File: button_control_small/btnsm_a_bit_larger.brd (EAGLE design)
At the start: 19 x 14.9 mm, 18 parts, among them IC1 TINY13V-10SSU, Q1 IRF8788

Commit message: Added version for heater canister
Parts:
- added LED1, LED3: (no value), eagle-ltspice:LED_SML0603
- added LED2, LED4: (no value), led:LED5MM
- added R3: 300, rcl:R0402
- moved OUT- 34.9 mm to (28.0, 34.5), turned to 180 degrees
- moved PAD2 34.9 mm to (30.7, 24.2), flipped to the bottom
- moved Q1 32.6 mm to (29.0, 30.3), flipped to the bottom, turned to 90 degrees
- moved IN- 24.6 mm to (28.0, 27.0), turned to 90 degrees
- moved C1 23.3 mm to (11.1, 33.3), flipped to the bottom
- moved R1 22.3 mm to (12.5, 31.2), flipped to the bottom, turned to 0 degrees
- moved R2 22.1 mm to (8.86, 31.2), flipped to the bottom, turned to 0 degrees
- moved IN+ 21.7 mm to (12.0, 34.5), turned to 180 degrees
- moved IC1 21.2 mm to (11.3, 26.8), flipped to the bottom
- moved C2 20.8 mm to (21.7, 27.0), flipped to the bottom, turned to 90 degrees
- moved PAD6 20.1 mm to (30.7, 22.0)
- moved PAD4 19.8 mm to (5.80, 31.6), flipped to the bottom
- moved PAD5 19.7 mm to (2.40, 23.9), flipped to the bottom
- moved PAD3 19.4 mm to (2.40, 21.9), flipped to the bottom
- moved U$3 18.3 mm to (19.6, 27.1), flipped to the bottom, turned to 270 degrees
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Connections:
- new net N$6: LED1.A, LED2.A, LED3.A, LED4.A, R3.2
- net N$3: now also R3.1
- net N$4: now also LED1.C, LED2.K, LED3.C, LED4.K
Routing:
- net N$4: track 13.5 -> 71.3 mm, vias 0 -> 5
- net N$6: track 0.00 -> 53.0 mm, vias 0 -> 2
- net N$2: track 2.28 -> 38.0 mm, vias 0 -> 2
- net VDD: track 14.7 -> 46.7 mm, vias 0 -> 1
- net N$3: track 9.79 -> 31.2 mm, vias 0 -> 2
- net MISO: track 2.19 -> 21.1 mm, vias 0 -> 1
- net GND: track 42.6 -> 57.9 mm, vias 0 -> 3
- net N$1: track 12.7 -> 1.72 mm
- net MOSI: track 1.89 -> 12.8 mm
- net SCK: track 2.64 -> 9.45 mm
- added copper zone on layer 16, net GND
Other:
- board size 19 x 14.9 mm -> 39.2 x 25.5 mm
- board text added: "+"
- board text added: "-"
- board text added: "B+"
- board text added: "B-"
- board text added: "BTN/GND"
- board text added: "BTN/MISO"
- board text added: "MOSI"
- board text added: "RST"
- board text added: "SCK"
- board text added: "VDD"

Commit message: Add files via upload
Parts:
- removed IC1: TINY13V-10SSU, atmel:8S1
- removed LED1, LED3: (no value), eagle-ltspice:LED_SML0603
- removed LED2, LED4: (no value), led:LED5MM
- removed PAD1, PAD2, PAD3, PAD4, PAD5, PAD6: (no value), wirepad:1,6/0,9
- added BTN1: BTN1, wirepad:1,6/0,9
- added BTN2: BNT2, wirepad:1,6/0,9
- added C4, C5: 100n, resistor:C0603
- added D1: (no value), SparkFun-LED:LED-TRICOLOR-5050
- added IC2: MEGA8-AI, atmel:TQFP32-08
- added J1: AVR_SPI_PROG_3X2NS, SparkFun-Connectors:2X3-NS
- added R10: 100k, rcl:R0402
- added R4, R5: 470, rcl:R0402
- added R6: 520, rcl:R0402
- added R7: 282k, rcl:R0402
- added R8: 470k, rcl:R0402
- added R9: 2.2k, rcl:R0402
- added RX: RX, wirepad:1,6/0,9
- added T1, T2: BC848, transistor-neu-to92:SOT23
- added TX: TX, wirepad:1,6/0,9
- added WTR: WATER, wirepad:1,6/0,9
- C2: value 0.33uF -> 100n
- C3: value 2.2uF -> 1uF; device resistor:C0603 -> resistor:C0805
- R3: value 300 -> 100k
- U$3: value TPS71550 -> TPS71533
- moved IN+ 26.2 mm to (36.0, 24.0), turned to 0 degrees
- moved OUT- 26.2 mm to (4.00, 24.0)
- moved R3 21.5 mm to (24.9, 28.7), flipped to the top, turned to 90 degrees
- moved Q1 20.3 mm to (9.88, 23.7), flipped to the top, turned to 180 degrees
- moved IN- 18.8 mm to (11.0, 19.0)
- moved OUT+ 18.7 mm to (28.9, 19.1)
- moved C3 13.9 mm to (31.3, 25.7), flipped to the top
- moved C1 9.64 mm to (10.1, 23.7), turned to 270 degrees
- moved U$3 9.62 mm to (29.1, 25.6), flipped to the top
- moved R2 7.99 mm to (11.7, 23.7), turned to 270 degrees
- moved R1 7.43 mm to (15.5, 24.4), flipped to the top, turned to 270 degrees
- moved C2 5.41 mm to (26.9, 25.5), flipped to the top
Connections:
- removed net N$1: IC1.3, R1.2
- removed net N$3: C2.1, IN+.1, OUT+.1, R3.1, U$3.4
- new net ADC0: IC2.23, R3.1, R7.2
- new net AREF: C5.2, IC2.20
- new net BTN1: BTN1.1, IC2.32
- new net N$13: T1.2, T2.1
- new net N$16: R10.2, R8.1, WTR.1
- new net N$17: R10.1, T1.1
- new net N$18: R9.1, T1.3
- new net N$7: D1.6, R4.2
- new net N$8: D1.4, R5.2
- new net PWM0: D1.3, IC2.10
- new net PWM1: D1.1, IC2.14
- new net PWM2: D1.2, IC2.13
- new net RX: IC2.30, R1.2, RX.1
- new net TX: IC2.31, TX.1
- new net VIN: C2.1, IN+.1, OUT+.1, R4.1, R5.1, R6.1, R7.1, R9.2, U$3.4
- new net WTR: IC2.1, T2.3
- net GND: now also BTN2.1, C4.2, C5.1, IC2.21, IC2.3, IC2.5, J1.6, R8.2, T2.2; no longer IC1.4, PAD6.1
- net MISO: now also IC2.16, J1.1; no longer IC1.6, PAD2.1
- net MOSI: now also IC2.15, J1.4; no longer IC1.5, PAD1.1
- net N$4: now also R3.2; no longer LED1.C, LED2.K, LED3.C, LED4.K
- net N$6: now also D1.5, R6.2; no longer LED1.A, LED2.A, LED3.A, LED4.A, R3.2
- net RST: now also IC2.29, J1.5; no longer IC1.1, PAD4.1
- net SCK: now also IC2.17, J1.3; no longer IC1.7, PAD3.1
- net VDD: now also C4.1, IC2.18, IC2.4, IC2.6, J1.2; no longer IC1.8, PAD5.1
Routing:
- net GND: track 57.9 -> 122.3 mm, vias 3 -> 2
- net MOSI: track 12.8 -> 66.4 mm
- net N$6: track 53.0 -> 4.80 mm, vias 2 -> 0
- net VIN: track 0.00 -> 39.1 mm, vias 0 -> 1
- net N$4: track 71.3 -> 35.5 mm, vias 5 -> 0
- net N$2: track 38.0 -> 3.09 mm, vias 2 -> 0
- net PWM1: track 0.00 -> 32.5 mm
- net RX: track 0.00 -> 32.3 mm, vias 0 -> 1
- net RST: track 8.76 -> 40.9 mm, vias 0 -> 2
- net N$3: track 31.2 -> 0.00 mm, vias 2 -> 0
- net PWM2: track 0.00 -> 30.7 mm
- net PWM0: track 0.00 -> 30.1 mm
- net MISO: track 21.1 -> 49.4 mm, vias 1 -> 0
- net ADC0: track 0.00 -> 28.1 mm, vias 0 -> 3
- net WTR: track 0.00 -> 25.9 mm, vias 0 -> 2
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- removed copper zone on layer 16, net GND
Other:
- board size 39.2 x 25.5 mm -> 41.4 x 41.4 mm
- board text removed: "BTN/GND"
- board text removed: "BTN/MISO"
- board text removed: "MOSI"
- board text removed: "RST"
- board text removed: "SCK"
- board text removed: "VDD"

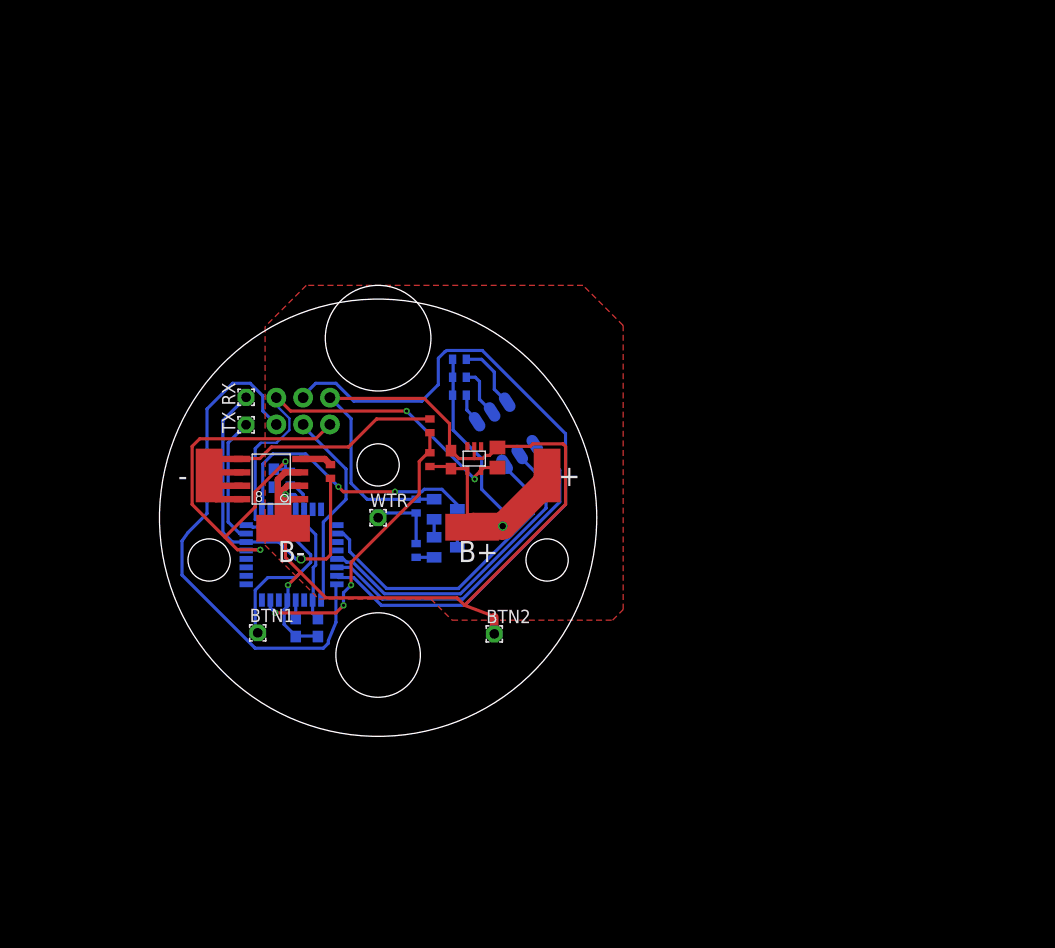
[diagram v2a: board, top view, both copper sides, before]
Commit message: Add files via upload
Developing a new version with better power consumption and capabilities
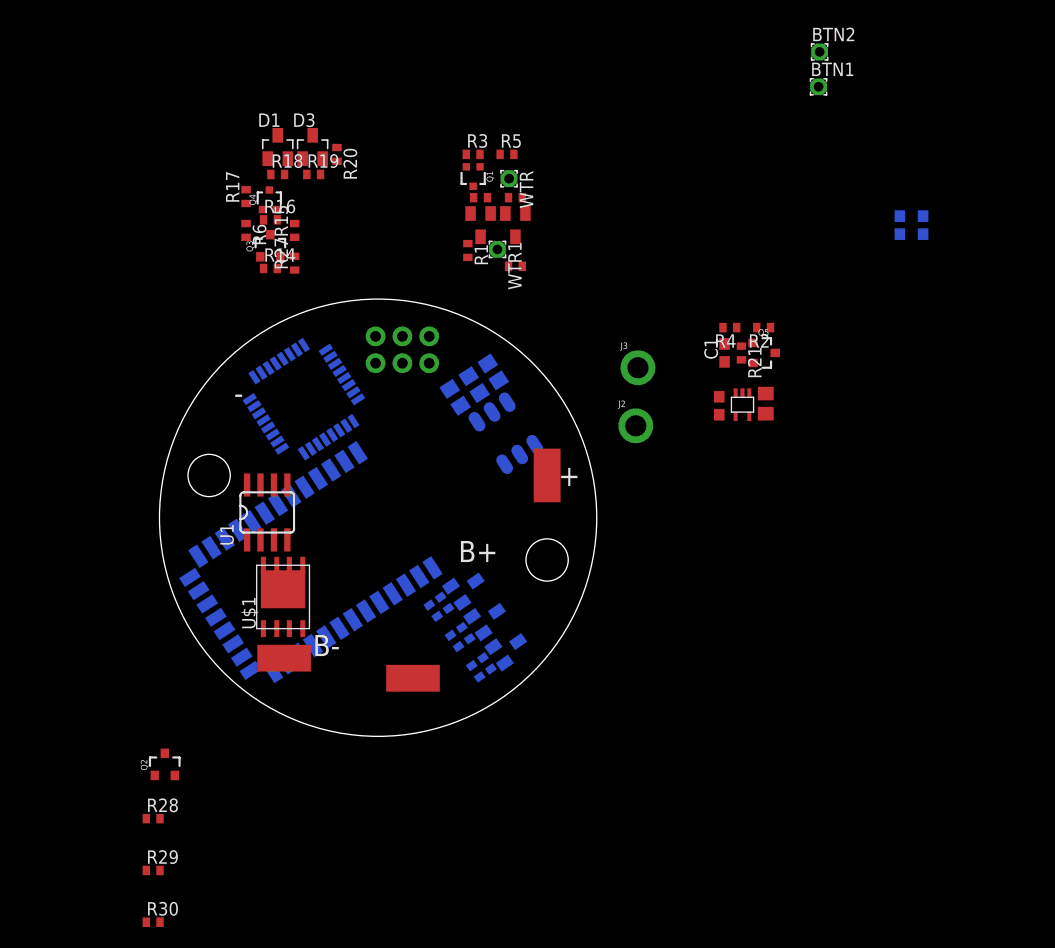
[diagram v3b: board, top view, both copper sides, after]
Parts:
- removed OUT-: OUT-, wirepad:SMD2,54-5,08
- removed RX: RX, wirepad:1,6/0,9
- removed TX: TX, wirepad:1,6/0,9
- added D2: (no value), SparkFun-LED:LED-TRICOLOR-5050
- added D3: BAT54, diode:SOT23
- added J2: OUT-, SparkFun-Connectors:1X01_2MM
- added J3: OUT+, SparkFun-Connectors:1X01_2MM
- added Q2, Q3, Q5: IRLML9301, SparkFun-DiscreteSemi:SOT23-3
- added Q4: 2N2007 (SOT323), SparkFun-DiscreteSemi:SOT323
- added R11, R12: 470, rcl:R0805
- added R13: 520, rcl:R0805
- added R14, R15, R16, R17, R20, R21, R22, R23, R28, R29, R30: 100k, rcl:R0402
- added R18, R19, R24, R25, R26, R27: 200, rcl:R0402
- added T3, T4, T5: BC848, transistor-neu-to92:SOT23
- added U$1: IRFH6200, IRFH6200:PQFN
- added U1: ACS711ELCTR-25AB-T, allegro:SOIC8
- added U2: HC_05, Bluetooth HC-05:BLUETOOTH_SMD
- added WTR1: WTR-PWR, wirepad:1,6/0,9
- D1: value (none) -> BAT54; device SparkFun-LED:LED-TRICOLOR-5050 -> diode:SOT23
- Q1: value IRF8788 -> 2N2007 (SOT323); device transistor-fet:SO-8 -> SparkFun-DiscreteSemi:SOT323
- R1: value 100R -> 100k
- R2: value 10K -> 282k
- R4: value 470 -> 100k
- R5: value 470 -> 200
- R6: value 520 -> 200
- R7: value 282k -> 100k
- WTR: value WATER -> WTR-IN
- moved BTN1 74.1 mm to (61.7, 60.8)
- moved C4 68.8 mm to (71.6, 47.7)
- moved C5 68.7 mm to (69.4, 47.7)
- moved BTN2 63.1 mm to (61.8, 64.1)
- moved R2 47.0 mm to (56.5, 38.0), flipped to the top, turned to 180 degrees
- moved C1 44.3 mm to (52.8, 35.6), flipped to the top, turned to 90 degrees
- moved R10 34.7 mm to (33.0, 50.3), flipped to the top, turned to 180 degrees
- moved D1 34.7 mm to (10.5, 55.1), flipped to the top, turned to 0 degrees
- moved Q1 34.4 mm to (29.0, 52.3)
- moved WTR 34.4 mm to (32.4, 52.1), turned to 270 degrees
- moved T1 31.2 mm to (33.0, 47.7), flipped to the top, turned to 180 degrees
- moved R8 29.8 mm to (29.7, 50.3), flipped to the top, turned to 180 degrees
- moved T2 27.1 mm to (29.7, 47.7), flipped to the top, turned to 180 degrees
- moved R3 26.0 mm to (29.0, 54.4), turned to 0 degrees
- moved C3 25.9 mm to (56.7, 30.8)
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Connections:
- removed net ADC0: IC2.23, R3.1, R7.2
- removed net PWM1: D1.1, IC2.14
- removed net PWM2: D1.2, IC2.13
- removed net RX: IC2.30, R1.2, RX.1
- removed net TX: IC2.31, TX.1
- removed net VIN: C2.1, IN+.1, OUT+.1, R4.1, R5.1, R6.1, R7.1, R9.2, U$3.4
- new net +12V: C2.1, IN+.1, OUT+.1, Q5.2, R11.1, R12.1, R13.1, R21.2, R27.1, R9.2, U$3.4, WTR1.1
- new net N$1: D2.2, R13.2
- new net N$10: Q4.1, R16.1, R18.2, R6.1
- new net N$11: C1.2, Q5.1, R21.1
- new net N$12: Q4.3, R17.2
- new net N$14: C1.1, IC2.24
- new net N$15: D1.1, R18.1
- new net N$19: D3.1, R19.1
- new net N$20: D1.3, D3.3, R20.1, U$1.4
- new net N$21: IC2.25, R19.2
- new net N$22: IC2.23, R2.2, R4.1
- new net N$23: Q5.3, R2.1
- new net N$24: D2.4, T5.3
- new net N$25: D2.6, T4.3
- new net N$26: D2.5, T3.3
- new net N$27: R23.1, R26.2, T5.1
- new net N$28: R22.1, R25.2, T4.1
- new net N$29: R24.2, R7.1, T3.1
- new net N$3: D2.3, R11.2
- new net N$30: IC2.14, R24.1
- new net N$31: IC2.13, R25.1
- new net N$32: Q3.2, R14.2, R27.2
- new net N$33: Q2.1, R28.1
- new net N$34: J2.1, U1.1, U1.2
- new net N$35: R29.2, R30.1
- new net N$36: Q2.3, R29.1, U1.8
- new net N$37: U1.7
- new net N$5: D2.1, R12.2
- new net N$9: Q3.3, R15.1, R6.2
- net GND: now also Q4.2, R15.2, R16.2, R20.2, R22.2, R23.2, R3.1, R30.2, R4.2, R7.2, T3.2, T4.2, T5.2, U$1.1, U$1.2, U$1.3, U1.5; no longer C1.2, Q1.1, Q1.3, R8.2, T2.2
- net N$2: now also T2.3; no longer Q1.4
- net N$4: now also Q1.3, R8.2, T2.2; no longer OUT-.1, Q1.5, Q1.6, Q1.7, Q1.8, R3.2
- net N$6: now also Q1.1, R3.2, R5.1; no longer D1.5, R6.2
- net N$7: now also Q3.1, R14.1, U$1.5, U$1.6, U$1.7, U$1.8, U$1.9, U1.3, U1.4; no longer D1.6, R4.2
- net N$8: no longer D1.4
- net PWM0: now also R26.1; no longer D1.3
- net RST: no longer C1.1, R2.1
- net VDD: now also Q2.2, R1.2, R17.1, R28.2; no longer R2.2
- net WTR: no longer T2.3
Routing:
- net GND: track 122.3 -> 0.00 mm, vias 2 -> 0
- net MOSI: track 66.4 -> 0.00 mm
- net VDD: track 58.9 -> 0.00 mm, vias 2 -> 0
- net MISO: track 49.4 -> 0.00 mm
- net RST: track 40.9 -> 0.00 mm, vias 2 -> 0
- net VIN: track 39.1 -> 0.00 mm, vias 1 -> 0
- net N$4: track 35.5 -> 0.00 mm
- net PWM1: track 32.5 -> 0.00 mm
- net RX: track 32.3 -> 0.00 mm, vias 1 -> 0
- net PWM2: track 30.7 -> 0.00 mm
- net PWM0: track 30.1 -> 0.00 mm
- net ADC0: track 28.1 -> 0.00 mm, vias 3 -> 0
- net WTR: track 25.9 -> 0.00 mm, vias 2 -> 0
- net SCK: track 19.3 -> 0.00 mm
- net BTN1: track 18.4 -> 0.00 mm
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- removed copper zone on layer 1, net GND

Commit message: Add files via upload
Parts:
- removed OUT+: OUT+, wirepad:SMD2,54-5,08
- removed U2: HC_05, Bluetooth HC-05:BLUETOOTH_SMD
- added C6: 10uF, resistor:C0805
- added JDY-08: JDY-08, jdy-08:JDY-08
- moved BTN2 65.1 mm to (15.5, 18.4)
- moved BTN1 60.6 mm to (15.5, 21.6)
- moved C4 54.1 mm to (28.6, 14.8), flipped to the top, turned to 90 degrees
- moved R3 53.1 mm to (13.5, 3.60), turned to 90 degrees
- moved R5 51.2 mm to (13.5, 6.70), turned to 90 degrees
- moved Q1 50.6 mm to (15.4, 3.60), turned to 270 degrees
- moved C5 50.5 mm to (28.6, 17.9), flipped to the top, turned to 270 degrees
- moved WTR 49.2 mm to (15.6, 5.90), turned to 0 degrees
- moved R8 47.6 mm to (17.3, 4.30), turned to 270 degrees
- moved R10 45.7 mm to (17.3, 7.40), turned to 270 degrees
- moved R30 45.7 mm to (11.3, 25.6), turned to 90 degrees
- moved T2 44.5 mm to (19.8, 4.30), turned to 270 degrees
- moved D1 43.2 mm to (12.4, 11.9), flipped to the bottom, turned to 90 degrees
- moved R1 42.7 mm to (22.1, 3.10), turned to 0 degrees
- moved T1 42.4 mm to (19.8, 7.40), turned to 270 degrees
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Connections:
- removed net N$2: R1.1, T2.3
- removed net N$8: R5.2
- removed net WTR: IC2.1
- new net ADC5: IC2.28, Q2.1, R28.1
- new net ADC6: IC2.19, U1.7
- new net ADC7: IC2.22, R29.2, R30.1
- new net N$38: IC2.30, JDY-08.19
- new net N$39: IC2.31, JDY-08.20
- new net PB6: IC2.7, R1.1, T2.3
- new net PB7: IC2.8, R5.2
- net +12V: now also J3.1; no longer OUT+.1
- net GND: now also C6.2, JDY-08.24
- net N$12: now also IC2.1
- net N$33: now also IC2.26, JDY-08.23; no longer Q2.1, R28.1
- net N$35: now also IC2.27, JDY-08.22; no longer R29.2, R30.1
- net N$37: now also IC2.2, JDY-08.6; no longer U1.7
- net VDD: now also C6.1, JDY-08.1
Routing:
- net GND: track 0.00 -> 176.2 mm, vias 0 -> 1
- net +12V: track 0.00 -> 117.5 mm
- net VDD: track 0.00 -> 109.9 mm, vias 0 -> 1
- net N$31: track 0.00 -> 30.2 mm, vias 0 -> 1
- net N$21: track 0.00 -> 29.1 mm, vias 0 -> 1
- net N$30: track 0.00 -> 26.9 mm, vias 0 -> 1
- net PWM0: track 0.00 -> 23.9 mm, vias 0 -> 1
- net N$12: track 0.00 -> 23.3 mm, vias 0 -> 1
- net RST: track 0.00 -> 22.9 mm, vias 0 -> 1
- net ADC6: track 0.00 -> 21.8 mm
- net ADC7: track 0.00 -> 21.8 mm
- net ADC5: track 0.00 -> 19.8 mm
- net N$7: track 0.00 -> 19.6 mm, vias 0 -> 1
- net N$22: track 0.00 -> 15.2 mm
- net PB6: track 0.00 -> 14.5 mm
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
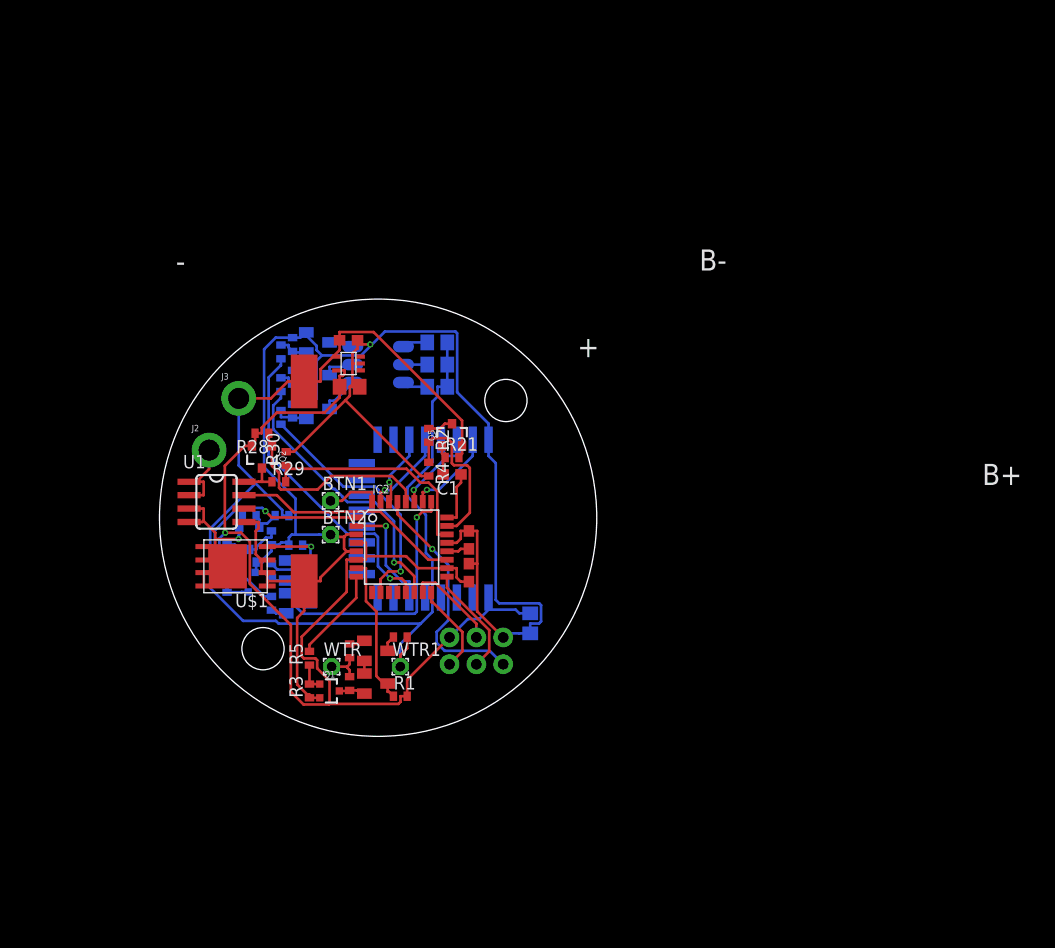
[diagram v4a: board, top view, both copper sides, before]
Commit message: Routed version with BT module
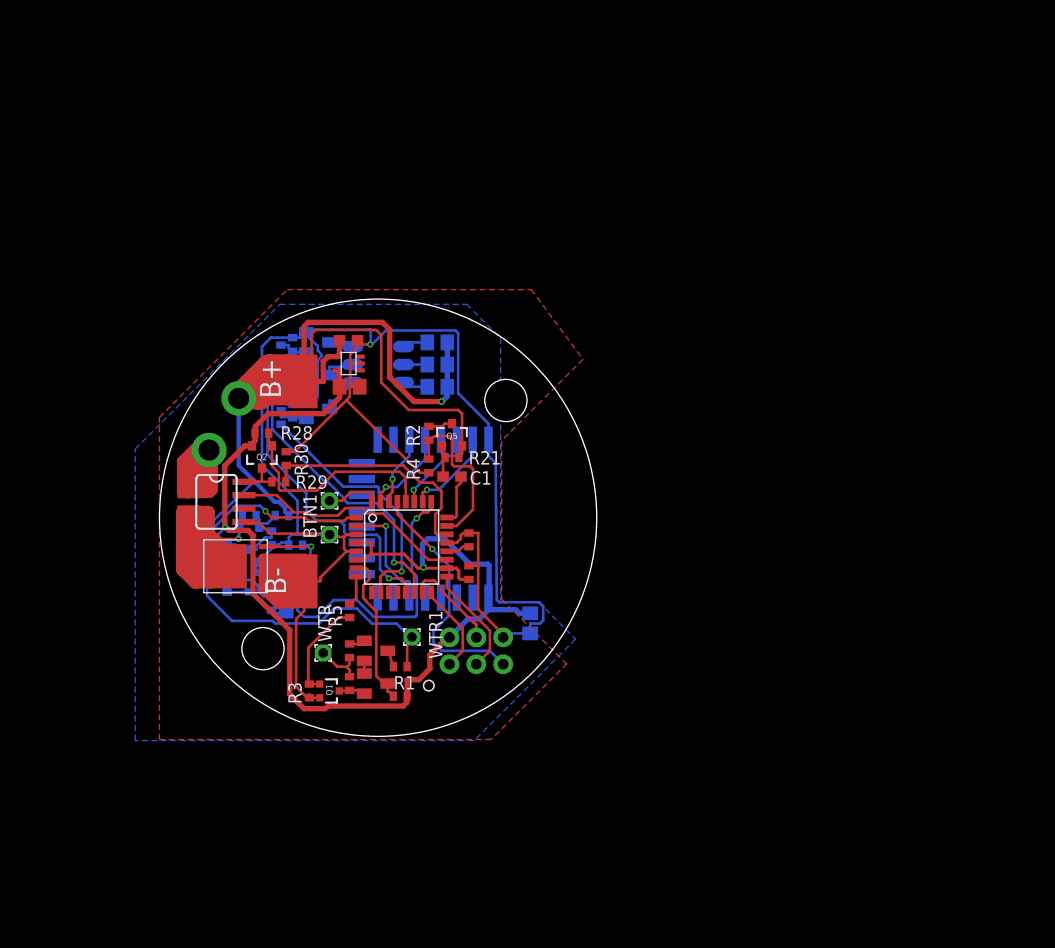
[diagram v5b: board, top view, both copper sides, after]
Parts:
- C4, C5: device resistor:C0603 -> resistor:C0402
- moved R5 5.89 mm to (17.3, 11.2)
- moved WTR1 3.01 mm to (23.2, 8.70)
- moved R9 2.80 mm to (22.1, 5.90)
- moved WTR 1.53 mm to (14.8, 7.20)
- moved R4 0.30 mm to (24.8, 24.9)
- moved C1 0.20 mm to (27.0, 23.9)
- moved R2 0.20 mm to (24.8, 28.0)
- moved BTN1 0.10 mm to (15.4, 21.6)
- moved BTN2 0.10 mm to (15.4, 18.4)
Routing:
- net N$7: track 19.6 -> 57.5 mm
- net GND: track 176.2 -> 212.9 mm
- net +12V: track 117.5 -> 133.1 mm, vias 0 -> 1
- net N$34: track 7.53 -> 22.6 mm
- net N$6: track 2.77 -> 9.65 mm
- net PB7: track 8.91 -> 2.98 mm
- net VDD: track 109.9 -> 106.5 mm, vias 1 -> 2
- net N$21: track 29.1 -> 31.3 mm
- net N$31: track 30.2 -> 31.7 mm
- net N$16: track 3.46 -> 4.79 mm
- net ADC5: track 19.8 -> 21.0 mm
- net N$12: track 23.3 -> 24.3 mm
- net ADC7: track 21.8 -> 22.6 mm
- net N$22: track 15.2 -> 15.8 mm
- net ADC6: track 21.8 -> 22.4 mm
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- added copper zone on layer 1, net GND
- added copper zone on layer 16, net GND
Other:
- board text removed: "+"
- board text removed: "-"
